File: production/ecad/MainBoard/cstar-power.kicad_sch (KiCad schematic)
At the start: 24 parts, among them IC1 LT8648SEV#PBF, U1 AZ1117IH-3.3TRG1

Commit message: added test points
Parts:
- added TP1: P12V, symbol Connector:TestPoint
- added TP2: P5V, symbol Connector:TestPoint
- added TP3: 5V, symbol Connector:TestPoint
- added TP4: GND, symbol Connector:TestPoint
- added TP5: P24V, symbol Connector:TestPoint
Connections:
- net GND: now also TP4.1
- net P12V: now also TP1.1
- net P24V: now also TP5.1
- net P3V3: now also TP3.1
- net P5V: now also TP2.1
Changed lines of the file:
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@@
   (junction (at 148.59 106.68) (diameter 0) (color 0 0 0 0)
   )
+  (junction (at 341.63 82.55) (diameter 0) (color 0 0 0 0)
+  )
   (junction (at 146.05 77.47) (diameter 0) (color 0 0 0 0)
   )
@@
   (junction (at 304.8 92.71) (diameter 0) (color 0 0 0 0)
   )
+  (junction (at 114.3 204.47) (diameter 0) (color 0 0 0 0)
+  )
   (junction (at 129.54 130.81) (diameter 0) (color 0 0 0 0)
   )
@@
   (junction (at 69.85 64.77) (diameter 0) (color 0 0 0 0)
   )
+  (junction (at 59.69 64.77) (diameter 0) (color 0 0 0 0)
+  )
   (junction (at 101.6 130.81) (diameter 0) (color 0 0 0 0)
   )
@@
   (junction (at 326.39 82.55) (diameter 0) (color 0 0 0 0)
   )
+  (junction (at 181.61 97.79) (diameter 0) (color 0 0 0 0)
+  )
   (junction (at 168.91 116.84) (diameter 0) (color 0 0 0 0)
   )
@@
   (junction (at 127 130.81) (diameter 0) (color 0 0 0 0)
   )
+  (junction (at 284.48 97.79) (diameter 0) (color 0 0 0 0)
+  )
   (junction (at 287.02 82.55) (diameter 0) (color 0 0 0 0)
   )
@@
     (stroke (width 0) (type default))
   )
+  (wire (pts (xy 181.61 97.79) (xy 179.07 97.79))
+    (stroke (width 0) (type default))
+  )
   (wire (pts (xy 99.06 128.27) (xy 99.06 130.81))
     (stroke (width 0) (type default))
@@
     (stroke (width 0) (type default))
   )
+  (wire (pts (xy 284.48 97.79) (xy 285.75 97.79))
+    (stroke (width 0) (type default))
+  )
   (wire (pts (xy 179.07 109.22) (xy 179.07 116.84))
     (stroke (width 0) (type default))
@@
     (stroke (width 0) (type default))
   )
-  (wire (pts (xy 337.82 82.55) (xy 344.17 82.55))
+  (wire (pts (xy 337.82 82.55) (xy 341.63 82.55))
     (stroke (width 0) (type default))
   )
@@
     (stroke (width 0) (type default))
   )
+  (wire (pts (xy 114.3 204.47) (xy 116.84 204.47))
+    (stroke (width 0) (type default))
+  )
   (wire (pts (xy 139.7 80.01) (xy 146.05 80.01))
     (stroke (width 0) (type default))
@@
     (stroke (width 0) (type default))
   )
+  (wire (pts (xy 341.63 77.47) (xy 341.63 82.55))
+    (stroke (width 0) (type default))
+  )
   (wire (pts (xy 326.39 86.36) (xy 326.39 82.55))
     (stroke (width 0) (type default))
@@
     (stroke (width 0) (type default))
   )
+  (wire (pts (xy 59.69 60.96) (xy 59.69 64.77))
+    (stroke (width 0) (type default))
+  )
   (wire (pts (xy 337.82 82.55) (xy 337.82 86.36))
     (stroke (width 0) (type default))
@@
     (stroke (width 0) (type default))
   )
+  (wire (pts (xy 114.3 199.39) (xy 114.3 204.47))
+    (stroke (width 0) (type default))
+  )
   (wire (pts (xy 283.21 77.47) (xy 287.02 77.47))
     (stroke (width 0) (type default))
   )
+  (wire (pts (xy 52.07 64.77) (xy 59.69 64.77))
+    (stroke (width 0) (type default))
+  )
   (wire (pts (xy 109.22 130.81) (xy 111.76 130.81))
     (stroke (width 0) (type default))
@@
     (stroke (width 0) (type default))
   )
-  (wire (pts (xy 111.76 204.47) (xy 116.84 204.47))
+  (wire (pts (xy 111.76 204.47) (xy 114.3 204.47))
     (stroke (width 0) (type default))
   )
@@
     (stroke (width 0) (type default))
   )
+  (wire (pts (xy 59.69 64.77) (xy 60.96 64.77))
+    (stroke (width 0) (type default))
+  )
   (wire (pts (xy 69.85 72.39) (xy 76.2 72.39))
     (stroke (width 0) (type default))
@@
     (stroke (width 0) (type default))
   )
-  (wire (pts (xy 55.88 64.77) (xy 60.96 64.77))
-    (stroke (width 0) (type default))
-  )
   (wire (pts (xy 58.42 106.68) (xy 58.42 114.3))
     (stroke (width 0) (type default))
@@
     (stroke (width 0) (type default))
   )
+  (wire (pts (xy 181.61 97.79) (xy 185.42 97.79))
+    (stroke (width 0) (type default))
+  )
   (wire (pts (xy 139.7 72.39) (xy 146.05 72.39))
     (stroke (width 0) (type default))
@@
     (stroke (width 0) (type default))
   )
-  (wire (pts (xy 179.07 97.79) (xy 185.42 97.79))
+  (wire (pts (xy 341.63 82.55) (xy 344.17 82.55))
     (stroke (width 0) (type default))
   )
@@
   )
   (wire (pts (xy 252.73 80.01) (xy 247.65 80.01))
+    (stroke (width 0) (type default))
+  )
+  (wire (pts (xy 181.61 92.71) (xy 181.61 97.79))
     (stroke (width 0) (type default))
   )
@@
     (effects (font (size 1.27 1.27)) (justify left bottom))
   )
-  (label "P24V" (at 55.88 64.77 0) (fields_autoplaced)
+  (label "P24V" (at 52.07 64.77 0) (fields_autoplaced)
     (effects (font (size 1.27 1.27)) (justify left bottom))
   )
@@
         (path "/7edd775e-47a6-46f9-8e16-808bdf3a0e15"
           (reference "R3") (unit 1)
+        )
+      )
+    )
+  )
+  (symbol (lib_id "Connector:TestPoint") (at 181.61 92.71 0) (unit 1)
+    (in_bom yes) (on_board yes) (dnp no)
+    (property "Reference" "TP1" (at 179.07 83.82 0)
+      (effects (font (size 1.27 1.27)) (justify left))
+    )
+    (property "Value" "P12V" (at 179.07 86.36 0)
+      (effects (font (size 1.27 1.27)) (justify left))
+    )
+    (property "Footprint" "" (at 186.69 92.71 0)
+      (effects (font (size 1.27 1.27)) hide)
+    )
+    (property "Datasheet" "~" (at 186.69 92.71 0)
+      (effects (font (size 1.27 1.27)) hide)
+    )
+    (pin "1")
+    (instances
+      (project "cstar-power"
+        (path "/7edd775e-47a6-46f9-8e16-808bdf3a0e15"
+          (reference "TP1") (unit 1)
         )
       )
@@
     )
   )
+  (symbol (lib_id "Connector:TestPoint") (at 114.3 199.39 0) (unit 1)
+    (in_bom yes) (on_board yes) (dnp no)
+    (property "Reference" "TP3" (at 115.57 194.31 0)
+      (effects (font (size 1.27 1.27)) (justify left))
+    )
+    (property "Value" "5V" (at 115.57 196.85 0)
+      (effects (font (size 1.27 1.27)) (justify left))
+    )
+    (property "Footprint" "" (at 119.38 199.39 0)
+      (effects (font (size 1.27 1.27)) hide)
+    )
+    (property "Datasheet" "~" (at 119.38 199.39 0)
+      (effects (font (size 1.27 1.27)) hide)
+    )
+    (pin "1")
+    (instances
+      (project "cstar-power"
+        (path "/7edd775e-47a6-46f9-8e16-808bdf3a0e15"
+          (reference "TP3") (unit 1)
+        )
+      )
+    )
+  )
   (symbol (lib_id "power:GND") (at 53.34 217.17 0) (unit 1)
     (in_bom yes) (on_board yes) (dnp no) (fields_autoplaced)
@@
         (path "/7edd775e-47a6-46f9-8e16-808bdf3a0e15"
           (reference "C5") (unit 1)
+        )
+      )
+    )
+  )
+  (symbol (lib_id "Connector:TestPoint") (at 59.69 60.96 0) (unit 1)
+    (in_bom yes) (on_board yes) (dnp no) (fields_autoplaced)
+    (property "Reference" "TP5" (at 62.23 56.388 0)
+      (effects (font (size 1.27 1.27)) (justify left))
+    )
+    (property "Value" "P24V" (at 62.23 58.928 0)
+      (effects (font (size 1.27 1.27)) (justify left))
+    )
+    (property "Footprint" "" (at 64.77 60.96 0)
+      (effects (font (size 1.27 1.27)) hide)
+    )
+    (property "Datasheet" "~" (at 64.77 60.96 0)
+      (effects (font (size 1.27 1.27)) hide)
+    )
+    (pin "1")
+    (instances
+      (project "cstar-power"
+        (path "/7edd775e-47a6-46f9-8e16-808bdf3a0e15"
+          (reference "TP5") (unit 1)
         )
       )
@@
     )
   )
+  (symbol (lib_id "Connector:TestPoint") (at 341.63 77.47 0) (unit 1)
+    (in_bom yes) (on_board yes) (dnp no)
+    (property "Reference" "TP2" (at 337.82 69.85 0)
+      (effects (font (size 1.27 1.27)) (justify left))
+    )
+    (property "Value" "P5V" (at 337.82 72.39 0)
+      (effects (font (size 1.27 1.27)) (justify left))
+    )
+    (property "Footprint" "" (at 346.71 77.47 0)
+      (effects (font (size 1.27 1.27)) hide)
+    )
+    (property "Datasheet" "~" (at 346.71 77.47 0)
+      (effects (font (size 1.27 1.27)) hide)
+    )
+    (pin "1")
+    (instances
+      (project "cstar-power"
+        (path "/7edd775e-47a6-46f9-8e16-808bdf3a0e15"
+          (reference "TP2") (unit 1)
+        )
+      )
+    )
+  )
   (symbol (lib_id "Device:L") (at 297.18 82.55 90) (unit 1)
     (in_bom yes) (on_board yes) (dnp no)
@@
         )
       )
+    )
+  )
+  (symbol (lib_id "Connector:TestPoint") (at 285.75 97.79 270) (unit 1)
+    (in_bom yes) (on_board yes) (dnp no) (fields_autoplaced)
+    (property "Reference" "TP4" (at 290.83 96.52 90)
+      (effects (font (size 1.27 1.27)) (justify left))
+    )
+    (property "Value" "GND" (at 290.83 99.06 90)
+      (effects (font (size 1.27 1.27)) (justify left))
+    )
+    (property "Footprint" "" (at 285.75 102.87 0)
+      (effects (font (size 1.27 1.27)) hide)
+    )
+    (property "Datasheet" "~" (at 285.75 102.87 0)
+      (effects (font (size 1.27 1.27)) hide)
+    )
+    (pin "1")
+    (instances
+      (project "cstar-power"
+        (path "/7edd775e-47a6-46f9-8e16-808bdf3a0e15"
+          (reference "TP4") (unit 1)
+        )
+      )

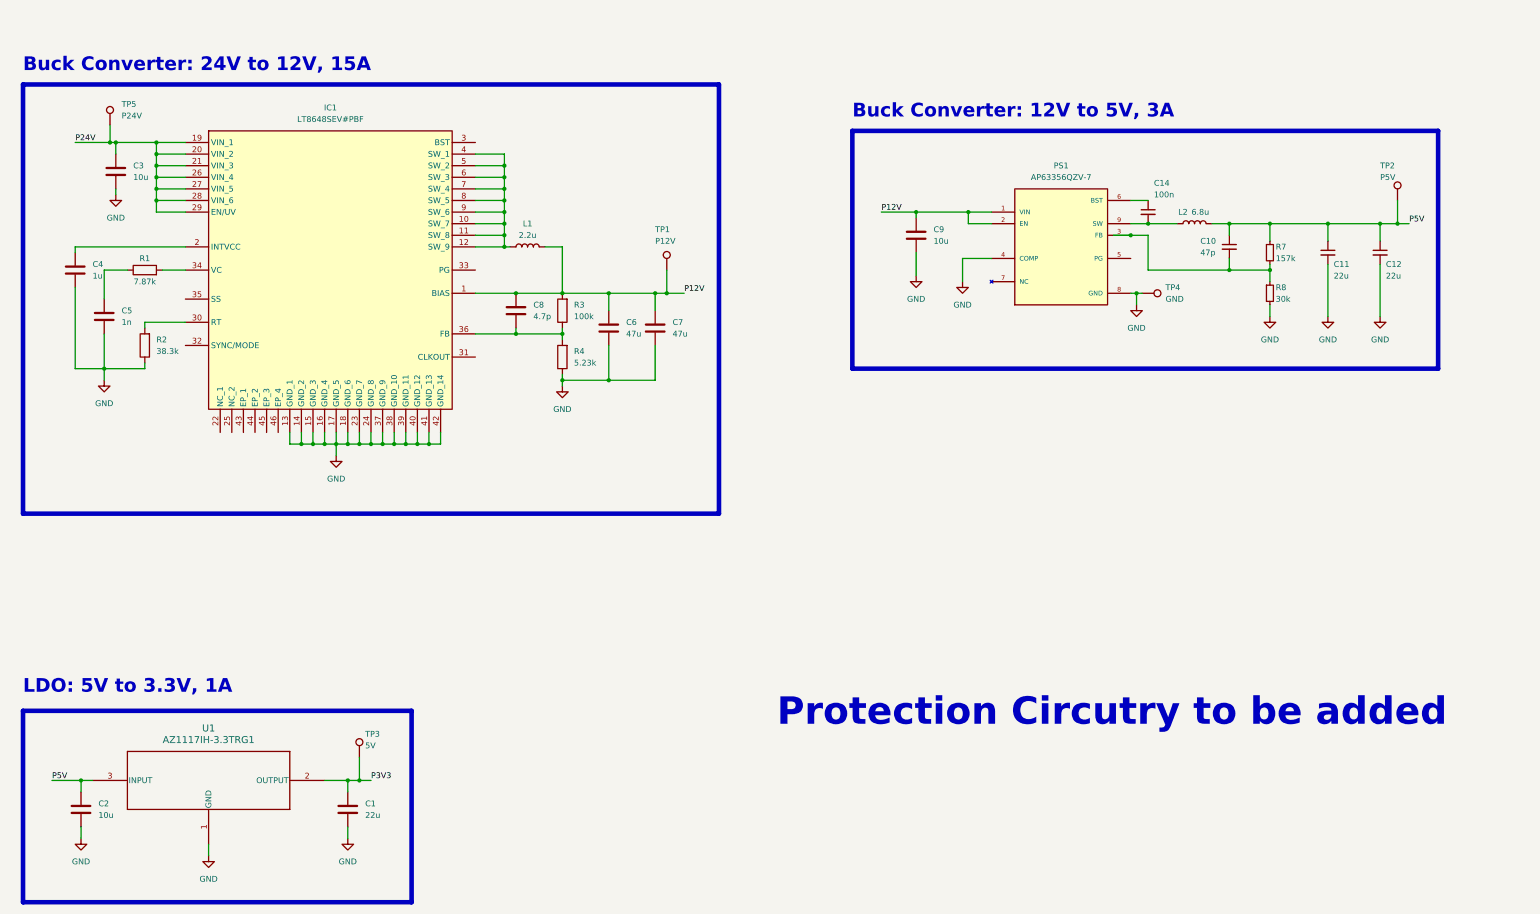
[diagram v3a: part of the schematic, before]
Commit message: Added global connections to power
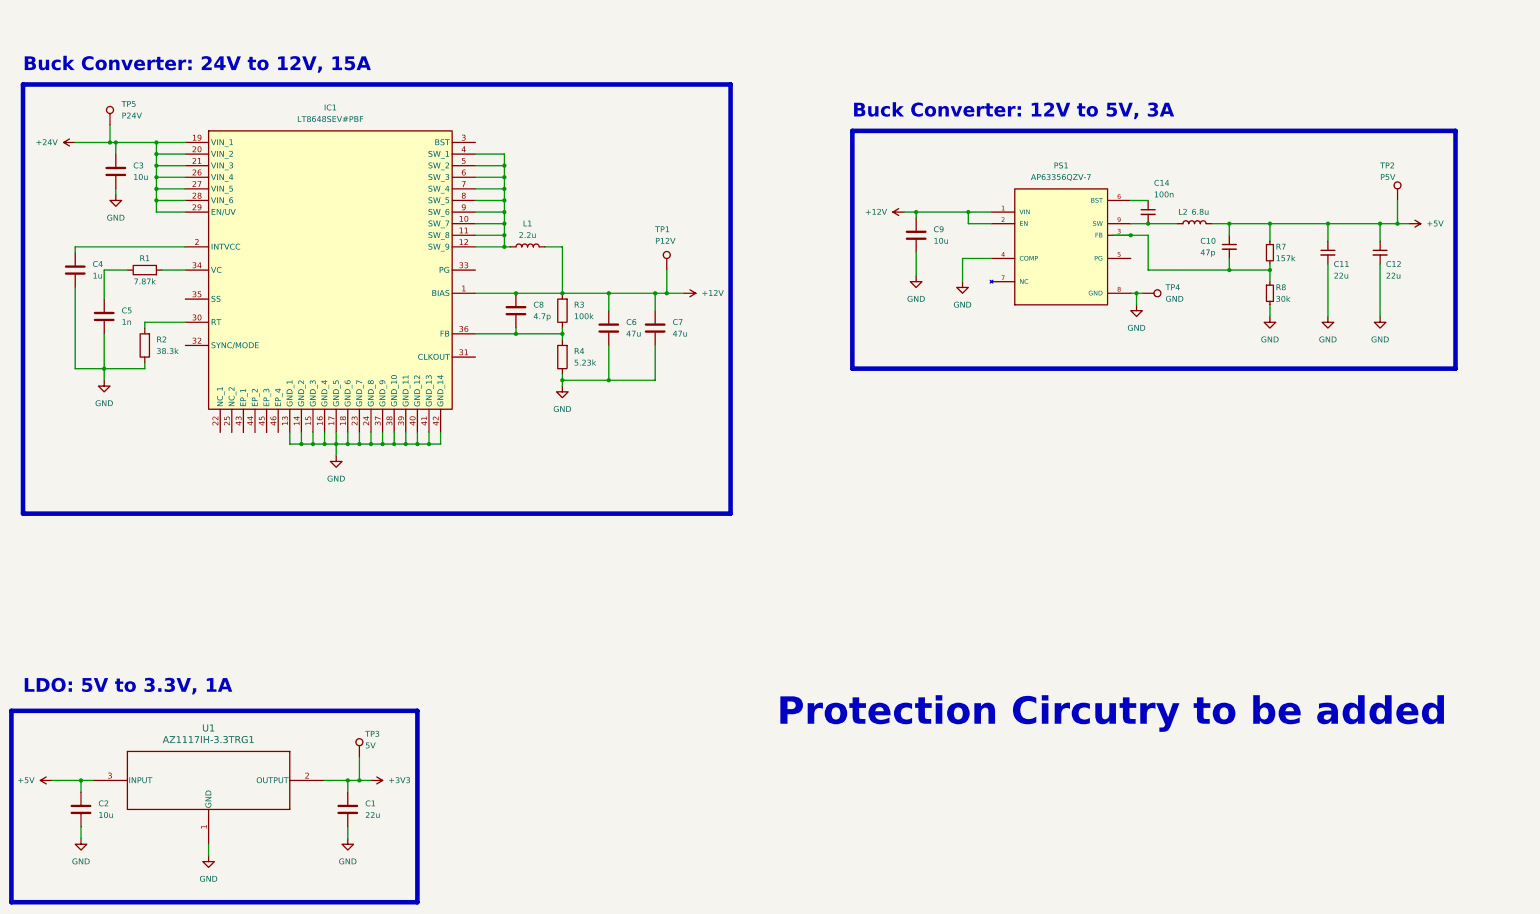
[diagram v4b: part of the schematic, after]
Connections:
- net P12V renamed +12V
- net P24V renamed +24V
- net P3V3 renamed +3V3
- net P5V renamed +5V
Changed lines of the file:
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@@
     (stroke (width 0) (type default))
   )
-  (wire (pts (xy 228.6 80.01) (xy 236.22 80.01))
+  (wire (pts (xy 233.68 80.01) (xy 236.22 80.01))
     (stroke (width 0) (type default))
   )
@@
     (fill (type none))
   )
-  (rectangle (start 40.64 189.23) (end 125.73 231.14)
+  (rectangle (start 38.1 189.23) (end 127 231.14)
     (stroke (width 1) (type default))
     (fill (type none))
   )
-  (rectangle (start 40.64 52.07) (end 193.04 146.05)
+  (rectangle (start 40.64 52.07) (end 195.58 146.05)
     (stroke (width 1) (type default))
     (fill (type none))
   )
-  (rectangle (start 222.25 62.23) (end 350.52 114.3)
+  (rectangle (start 222.25 62.23) (end 354.33 114.3)
     (stroke (width 1) (type default))
     (fill (type none))
@@
     (effects (font (size 3 3) (thickness 0.6) bold) (justify left bottom))
   )
-  (label "P3V3" (at 116.84 204.47 0) (fields_autoplaced)
-    (effects (font (size 1.27 1.27)) (justify left bottom))
-  )
-  (label "P12V" (at 228.6 80.01 0) (fields_autoplaced)
-    (effects (font (size 1.27 1.27)) (justify left bottom))
-  )
-  (label "P5V" (at 46.99 204.47 0) (fields_autoplaced)
-    (effects (font (size 1.27 1.27)) (justify left bottom))
-  )
-  (label "P24V" (at 52.07 64.77 0) (fields_autoplaced)
-    (effects (font (size 1.27 1.27)) (justify left bottom))
-  )
-  (label "P12V" (at 185.42 97.79 0) (fields_autoplaced)
-    (effects (font (size 1.27 1.27)) (justify left bottom))
-  )
-  (label "P5V" (at 344.17 82.55 0) (fields_autoplaced)
-    (effects (font (size 1.27 1.27)) (justify left bottom))
-  )
   (symbol (lib_id "Device:C") (at 53.34 210.82 0) (unit 1)
     (in_bom yes) (on_board yes) (dnp no) (fields_autoplaced)
@@
         (path "/7edd775e-47a6-46f9-8e16-808bdf3a0e15"
           (reference "#PWR08") (unit 1)
+        )
+      )
+    )
+  )
+  (symbol (lib_id "power:+12V") (at 233.68 80.01 90) (unit 1)
+    (in_bom yes) (on_board yes) (dnp no)
+    (property "Reference" "#PWR019" (at 237.49 80.01 0)
+      (effects (font (size 1.27 1.27)) hide)
+    )
+    (property "Value" "+12V" (at 229.87 80.01 90)
+      (effects (font (size 1.27 1.27)) (justify left))
+    )
+    (property "Footprint" "" (at 233.68 80.01 0)
+      (effects (font (size 1.27 1.27)) hide)
+    )
+    (property "Datasheet" "" (at 233.68 80.01 0)
+      (effects (font (size 1.27 1.27)) hide)
+    )
+    (pin "1")
+    (instances
+      (project "cstar-power"
+        (path "/7edd775e-47a6-46f9-8e16-808bdf3a0e15"
+          (reference "#PWR019") (unit 1)
         )
       )
@@
         (path "/7edd775e-47a6-46f9-8e16-808bdf3a0e15"
           (reference "C1") (unit 1)
+        )
+      )
+    )
+  )
+  (symbol (lib_id "power:+5V") (at 344.17 82.55 270) (unit 1)
+    (in_bom yes) (on_board yes) (dnp no) (fields_autoplaced)
+    (property "Reference" "#PWR014" (at 340.36 82.55 0)
+      (effects (font (size 1.27 1.27)) hide)
+    )
+    (property "Value" "+5V" (at 347.98 82.55 90)
+      (effects (font (size 1.27 1.27)) (justify left))
+    )
+    (property "Footprint" "" (at 344.17 82.55 0)
+      (effects (font (size 1.27 1.27)) hide)
+    )
+    (property "Datasheet" "" (at 344.17 82.55 0)
+      (effects (font (size 1.27 1.27)) hide)
+    )
+    (pin "1")
+    (instances
+      (project "cstar-power"
+        (path "/7edd775e-47a6-46f9-8e16-808bdf3a0e15"
+          (reference "#PWR014") (unit 1)
         )
       )
@@
     )
   )
+  (symbol (lib_id "power:+3V3") (at 116.84 204.47 270) (unit 1)
+    (in_bom yes) (on_board yes) (dnp no) (fields_autoplaced)
+    (property "Reference" "#PWR016" (at 113.03 204.47 0)
+      (effects (font (size 1.27 1.27)) hide)
+    )
+    (property "Value" "+3V3" (at 120.65 204.47 90)
+      (effects (font (size 1.27 1.27)) (justify left))
+    )
+    (property "Footprint" "" (at 116.84 204.47 0)
+      (effects (font (size 1.27 1.27)) hide)
+    )
+    (property "Datasheet" "" (at 116.84 204.47 0)
+      (effects (font (size 1.27 1.27)) hide)
+    )
+    (pin "1")
+    (instances
+      (project "cstar-power"
+        (path "/7edd775e-47a6-46f9-8e16-808bdf3a0e15"
+          (reference "#PWR016") (unit 1)
+        )
+      )
+    )
+  )
+  (symbol (lib_id "power:+12V") (at 185.42 97.79 270) (unit 1)
+    (in_bom yes) (on_board yes) (dnp no) (fields_autoplaced)
+    (property "Reference" "#PWR018" (at 181.61 97.79 0)
+      (effects (font (size 1.27 1.27)) hide)
+    )
+    (property "Value" "+12V" (at 189.23 97.79 90)
+      (effects (font (size 1.27 1.27)) (justify left))
+    )
+    (property "Footprint" "" (at 185.42 97.79 0)
+      (effects (font (size 1.27 1.27)) hide)
+    )
+    (property "Datasheet" "" (at 185.42 97.79 0)
+      (effects (font (size 1.27 1.27)) hide)
+    )
+    (pin "1")
+    (instances
+      (project "cstar-power"
+        (path "/7edd775e-47a6-46f9-8e16-808bdf3a0e15"
+          (reference "#PWR018") (unit 1)
+        )
+      )
+    )
+  )
   (symbol (lib_id "power:GND") (at 53.34 217.17 0) (unit 1)
     (in_bom yes) (on_board yes) (dnp no) (fields_autoplaced)
@@
     )
   )
+  (symbol (lib_id "power:+5V") (at 46.99 204.47 90) (unit 1)
+    (in_bom yes) (on_board yes) (dnp no) (fields_autoplaced)
+    (property "Reference" "#PWR015" (at 50.8 204.47 0)
+      (effects (font (size 1.27 1.27)) hide)
+    )
+    (property "Value" "+5V" (at 43.18 204.47 90)
+      (effects (font (size 1.27 1.27)) (justify left))
+    )
+    (property "Footprint" "" (at 46.99 204.47 0)
+      (effects (font (size 1.27 1.27)) hide)
+    )
+    (property "Datasheet" "" (at 46.99 204.47 0)
+      (effects (font (size 1.27 1.27)) hide)
+    )
+    (pin "1")
+    (instances
+      (project "cstar-power"
+        (path "/7edd775e-47a6-46f9-8e16-808bdf3a0e15"
+          (reference "#PWR015") (unit 1)
+        )
+      )
+    )
+  )
   (symbol (lib_id "power:GND") (at 60.96 76.2 0) (unit 1)
     (in_bom yes) (on_board yes) (dnp no) (fields_autoplaced)
@@
         )
       )
+    )
+  )
+  (symbol (lib_id "power:+24V") (at 52.07 64.77 90) (unit 1)
+    (in_bom yes) (on_board yes) (dnp no) (fields_autoplaced)
+    (property "Reference" "#PWR017" (at 55.88 64.77 0)
+      (effects (font (size 1.27 1.27)) hide)
+    )
+    (property "Value" "+24V" (at 48.26 64.77 90)
+      (effects (font (size 1.27 1.27)) (justify left))
+    )
+    (property "Footprint" "" (at 52.07 64.77 0)
+      (effects (font (size 1.27 1.27)) hide)
+    )
+    (property "Datasheet" "" (at 52.07 64.77 0)
+      (effects (font (size 1.27 1.27)) hide)
+    )
+    (pin "1")
+    (instances
+      (project "cstar-power"
+        (path "/7edd775e-47a6-46f9-8e16-808bdf3a0e15"
+          (reference "#PWR017") (unit 1)
+        )
+      )
